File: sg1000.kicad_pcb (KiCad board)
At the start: 2 copper layers, 64 parts, among them CN1 Conn_01x07_Female, J1 USB-B1HSB6, J2 RCJ-014, J3 RCJ-013, Q1 2n4401, Q1c1 2n3906, SW1 Pause Key, SW2 Power Toggle, U1 SG-1000-Cart, U10 PLCCZ80, U100 74HCT574, U101 74HCT574, U102 74HCT574, U103 AS6C62256-DIP, U11 AS6C62256-DIP, U12 TMS9918A, U13 74LS139, U16 74LS32, U18 74LS257, U21 74LS257, U3 SN76489AN, U99 74HCT04, X2 10.73863MHz

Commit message: This routing is gonna kill me
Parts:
- moved U16 103.4 mm to (65.6, 137.0), turned to -90 degrees
- moved U13 22.0 mm to (68.2, 149.2), turned to -90 degrees
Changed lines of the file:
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@@
   )
   (footprint "Package_DIP:DIP-16_W7.62mm_LongPads" (layer "F.Cu")
-    (at 76.962 129.032 180)
+    (at 68.16 149.175 -90)
     (descr "16-lead though-hole mounted DIP package, row spacing 7.62 mm (300 mils), LongPads")
     (tags "THT DIP DIL PDIP 2.54mm 7.62mm 300mil LongPads")
@@
     (property "Sheetname" "")
     (attr through_hole)
-    (fp_text reference "U13" (at 3.81 -2.33) (layer "F.SilkS")
+    (fp_text reference "U13" (at 3.81 -2.33 -270) (layer "F.SilkS")
       (effects (font (size 1 1) (thickness 0.15)))
     )
-    (fp_text value "74LS139" (at 3.81 20.11) (layer "F.Fab")
+    (fp_text value "74LS139" (at 3.81 20.11 -270) (layer "F.Fab")
       (effects (font (size 1 1) (thickness 0.15)))
     )
-    (fp_text user "${REFERENCE}" (at 3.81 8.89) (layer "F.Fab")
+    (fp_text user "${REFERENCE}" (at 3.81 8.89 -270) (layer "F.Fab")
       (effects (font (size 1 1) (thickness 0.15)))
     )
@@
     (fp_line (start 6.985 19.05) (end 0.635 19.05) (layer "F.Fab") (width 0.1))
     (fp_line (start 6.985 -1.27) (end 6.985 19.05) (layer "F.Fab") (width 0.1))
-    (pad "1" thru_hole rect (at 0 0 180) (size 2.4 1.6) (drill 0.8) (layers *.Cu *.Mask)
+    (pad "1" thru_hole rect (at 0 0 270) (size 2.4 1.6) (drill 0.8) (layers *.Cu *.Mask)
       (net 43 "/~{MREQ}") (pinfunction "E") (pintype "input"))
-    (pad "2" thru_hole oval (at 0 2.54 180) (size 2.4 1.6) (drill 0.8) (layers *.Cu *.Mask)
+    (pad "2" thru_hole oval (at 0 2.54 270) (size 2.4 1.6) (drill 0.8) (layers *.Cu *.Mask)
       (net 22 "/A14") (pinfunction "A0") (pintype "input"))
-    (pad "3" thru_hole oval (at 0 5.08 180) (size 2.4 1.6) (drill 0.8) (layers *.Cu *.Mask)
+    (pad "3" thru_hole oval (at 0 5.08 270) (size 2.4 1.6) (drill 0.8) (layers *.Cu *.Mask)
       (net 24 "/A15") (pinfunction "A1") (pintype "input"))
-    (pad "4" thru_hole oval (at 0 7.62 180) (size 2.4 1.6) (drill 0.8) (layers *.Cu *.Mask)
+    (pad "4" thru_hole oval (at 0 7.62 270) (size 2.4 1.6) (drill 0.8) (layers *.Cu *.Mask)
       (net 99 "unconnected-(U13-Pad4)") (pinfunction "O0") (pintype "output+no_connect"))
-    (pad "5" thru_hole oval (at 0 10.16 180) (size 2.4 1.6) (drill 0.8) (layers *.Cu *.Mask)
+    (pad "5" thru_hole oval (at 0 10.16 270) (size 2.4 1.6) (drill 0.8) (layers *.Cu *.Mask)
       (net 97 "unconnected-(U13-Pad5)") (pinfunction "O1") (pintype "output+no_connect"))
-    (pad "6" thru_hole oval (at 0 12.7 180) (size 2.4 1.6) (drill 0.8) (layers *.Cu *.Mask)
+    (pad "6" thru_hole oval (at 0 12.7 270) (size 2.4 1.6) (drill 0.8) (layers *.Cu *.Mask)
       (net 45 "/~{EXM1}") (pinfunction "O2") (pintype "output"))
-    (pad "7" thru_hole oval (at 0 15.24 180) (size 2.4 1.6) (drill 0.8) (layers *.Cu *.Mask)
+    (pad "7" thru_hole oval (at 0 15.24 270) (size 2.4 1.6) (drill 0.8) (layers *.Cu *.Mask)
       (net 44 "Net-(R9-Pad2)") (pinfunction "O3") (pintype "output"))
-    (pad "8" thru_hole oval (at 0 17.78 180) (size 2.4 1.6) (drill 0.8) (layers *.Cu *.Mask)
+    (pad "8" thru_hole oval (at 0 17.78 270) (size 2.4 1.6) (drill 0.8) (layers *.Cu *.Mask)
       (net 1 "GND") (pinfunction "GND") (pintype "power_in"))
-    (pad "9" thru_hole oval (at 7.62 17.78 180) (size 2.4 1.6) (drill 0.8) (layers *.Cu *.Mask)
+    (pad "9" thru_hole oval (at 7.62 17.78 270) (size 2.4 1.6) (drill 0.8) (layers *.Cu *.Mask)
       (net 51 "/~{KB_SEL}") (pinfunction "O3") (pintype "output"))
-    (pad "10" thru_hole oval (at 7.62 15.24 180) (size 2.4 1.6) (drill 0.8) (layers *.Cu *.Mask)
+    (pad "10" thru_hole oval (at 7.62 15.24 270) (size 2.4 1.6) (drill 0.8) (layers *.Cu *.Mask)
       (net 50 "Net-(U13-Pad10)") (pinfunction "O2") (pintype "output"))
-    (pad "11" thru_hole oval (at 7.62 12.7 180) (size 2.4 1.6) (drill 0.8) (layers *.Cu *.Mask)
+    (pad "11" thru_hole oval (at 7.62 12.7 270) (size 2.4 1.6) (drill 0.8) (layers *.Cu *.Mask)
       (net 49 "Net-(R4-Pad1)") (pinfunction "O1") (pintype "output"))
-    (pad "12" thru_hole oval (at 7.62 10.16 180) (size 2.4 1.6) (drill 0.8) (layers *.Cu *.Mask)
+    (pad "12" thru_hole oval (at 7.62 10.16 270) (size 2.4 1.6) (drill 0.8) (layers *.Cu *.Mask)
       (net 98 "unconnected-(U13-Pad12)") (pinfunction "O0") (pintype "output+no_connect"))
-    (pad "13" thru_hole oval (at 7.62 7.62 180) (size 2.4 1.6) (drill 0.8) (layers *.Cu *.Mask)
+    (pad "13" thru_hole oval (at 7.62 7.62 270) (size 2.4 1.6) (drill 0.8) (layers *.Cu *.Mask)
       (net 18 "/A7") (pinfunction "A1") (pintype "input"))
-    (pad "14" thru_hole oval (at 7.62 5.08 180) (size 2.4 1.6) (drill 0.8) (layers *.Cu *.Mask)
+    (pad "14" thru_hole oval (at 7.62 5.08 270) (size 2.4 1.6) (drill 0.8) (layers *.Cu *.Mask)
       (net 20 "/A6") (pinfunction "A0") (pintype "input"))
-    (pad "15" thru_hole oval (at 7.62 2.54 180) (size 2.4 1.6) (drill 0.8) (layers *.Cu *.Mask)
+    (pad "15" thru_hole oval (at 7.62 2.54 270) (size 2.4 1.6) (drill 0.8) (layers *.Cu *.Mask)
       (net 35 "/~{IORQ}") (pinfunction "E") (pintype "input"))
-    (pad "16" thru_hole oval (at 7.62 0 180) (size 2.4 1.6) (drill 0.8) (layers *.Cu *.Mask)
+    (pad "16" thru_hole oval (at 7.62 0 270) (size 2.4 1.6) (drill 0.8) (layers *.Cu *.Mask)
       (net 2 "+5V") (pinfunction "VCC") (pintype "power_in"))
     (model "${KICAD6_3DMODEL_DIR}/Package_DIP.3dshapes/DIP-16_W7.62mm.wrl"
@@
   )
   (footprint "Package_DIP:DIP-14_W7.62mm_LongPads" (layer "F.Cu")
-    (at 165.085 108.58)
+    (at 65.62 137 -90)
     (descr "14-lead though-hole mounted DIP package, row spacing 7.62 mm (300 mils), LongPads")
     (tags "THT DIP DIL PDIP 2.54mm 7.62mm 300mil LongPads")
@@
     (property "Sheetname" "")
     (attr through_hole)
-    (fp_text reference "U16" (at 3.81 -2.33) (layer "F.SilkS")
+    (fp_text reference "U16" (at 3.81 -2.33 90) (layer "F.SilkS")
       (effects (font (size 1 1) (thickness 0.15)))
     )
-    (fp_text value "74LS32" (at 3.81 17.57) (layer "F.Fab")
+    (fp_text value "74LS32" (at 3.81 17.57 90) (layer "F.Fab")
       (effects (font (size 1 1) (thickness 0.15)))
     )
-    (fp_text user "${REFERENCE}" (at 3.81 7.62) (layer "F.Fab")
+    (fp_text user "${REFERENCE}" (at 3.81 7.62 90) (layer "F.Fab")
       (effects (font (size 1 1) (thickness 0.15)))
     )
@@
     (fp_line (start 0.635 16.51) (end 0.635 -0.27) (layer "F.Fab") (width 0.1))
     (fp_line (start 6.985 16.51) (end 0.635 16.51) (layer "F.Fab") (width 0.1))
-    (pad "1" thru_hole rect (at 0 0) (size 2.4 1.6) (drill 0.8) (layers *.Cu *.Mask)
+    (pad "1" thru_hole rect (at 0 0 270) (size 2.4 1.6) (drill 0.8) (layers *.Cu *.Mask)
       (net 50 "Net-(U13-Pad10)") (pintype "input"))
-    (pad "2" thru_hole oval (at 0 2.54) (size 2.4 1.6) (drill 0.8) (layers *.Cu *.Mask)
+    (pad "2" thru_hole oval (at 0 2.54 270) (size 2.4 1.6) (drill 0.8) (layers *.Cu *.Mask)
       (net 29 "/~{RD}") (pintype "input"))
-    (pad "3" thru_hole oval (at 0 5.08) (size 2.4 1.6) (drill 0.8) (layers *.Cu *.Mask)
+    (pad "3" thru_hole oval (at 0 5.08 270) (size 2.4 1.6) (drill 0.8) (layers *.Cu *.Mask)
       (net 54 "/~{VDP_RD}") (pintype "output"))
-    (pad "4" thru_hole oval (at 0 7.62) (size 2.4 1.6) (drill 0.8) (layers *.Cu *.Mask)
+    (pad "4" thru_hole oval (at 0 7.62 270) (size 2.4 1.6) (drill 0.8) (layers *.Cu *.Mask)
       (net 50 "Net-(U13-Pad10)") (pintype "input"))
-    (pad "5" thru_hole oval (at 0 10.16) (size 2.4 1.6) (drill 0.8) (layers *.Cu *.Mask)
+    (pad "5" thru_hole oval (at 0 10.16 270) (size 2.4 1.6) (drill 0.8) (layers *.Cu *.Mask)
       (net 30 "/~{WR}") (pintype "input"))
-    (pad "6" thru_hole oval (at 0 12.7) (size 2.4 1.6) (drill 0.8) (layers *.Cu *.Mask)
+    (pad "6" thru_hole oval (at 0 12.7 270) (size 2.4 1.6) (drill 0.8) (layers *.Cu *.Mask)
       (net 52 "/~{VDP_WR}") (pintype "output"))
-    (pad "7" thru_hole oval (at 0 15.24) (size 2.4 1.6) (drill 0.8) (layers *.Cu *.Mask)
+    (pad "7" thru_hole oval (at 0 15.24 270) (size 2.4 1.6) (drill 0.8) (layers *.Cu *.Mask)
       (net 1 "GND") (pinfunction "GND") (pintype "power_in"))
-    (pad "8" thru_hole oval (at 7.62 15.24) (size 2.4 1.6) (drill 0.8) (layers *.Cu *.Mask)
+    (pad "8" thru_hole oval (at 7.62 15.24 270) (size 2.4 1.6) (drill 0.8) (layers *.Cu *.Mask)
       (net 55 "Net-(R15-Pad2)") (pintype "output"))
-    (pad "9" thru_hole oval (at 7.62 12.7) (size 2.4 1.6) (drill 0.8) (layers *.Cu *.Mask)
+    (pad "9" thru_hole oval (at 7.62 12.7 270) (size 2.4 1.6) (drill 0.8) (layers *.Cu *.Mask)
       (net 51 "/~{KB_SEL}") (pintype "input"))
-    (pad "10" thru_hole oval (at 7.62 10.16) (size 2.4 1.6) (drill 0.8) (layers *.Cu *.Mask)
+    (pad "10" thru_hole oval (at 7.62 10.16 270) (size 2.4 1.6) (drill 0.8) (layers *.Cu *.Mask)
       (net 29 "/~{RD}") (pintype "input"))
-    (pad "11" thru_hole oval (at 7.62 7.62) (size 2.4 1.6) (drill 0.8) (layers *.Cu *.Mask)
+    (pad "11" thru_hole oval (at 7.62 7.62 270) (size 2.4 1.6) (drill 0.8) (layers *.Cu *.Mask)
       (net 53 "/~{EXM2}") (pintype "output"))
-    (pad "12" thru_hole oval (at 7.62 5.08) (size 2.4 1.6) (drill 0.8) (layers *.Cu *.Mask)
+    (pad "12" thru_hole oval (at 7.62 5.08 270) (size 2.4 1.6) (drill 0.8) (layers *.Cu *.Mask)
       (net 24 "/A15") (pintype "input"))
-    (pad "13" thru_hole oval (at 7.62 2.54) (size 2.4 1.6) (drill 0.8) (layers *.Cu *.Mask)
+    (pad "13" thru_hole oval (at 7.62 2.54 270) (size 2.4 1.6) (drill 0.8) (layers *.Cu *.Mask)
       (net 43 "/~{MREQ}") (pintype "input"))
-    (pad "14" thru_hole oval (at 7.62 0) (size 2.4 1.6) (drill 0.8) (layers *.Cu *.Mask)
+    (pad "14" thru_hole oval (at 7.62 0 270) (size 2.4 1.6) (drill 0.8) (layers *.Cu *.Mask)
       (net 2 "+5V") (pinfunction "VCC") (pintype "power_in"))
     (model "${KICAD6_3DMODEL_DIR}/Package_DIP.3dshapes/DIP-14_W7.62mm.wrl"

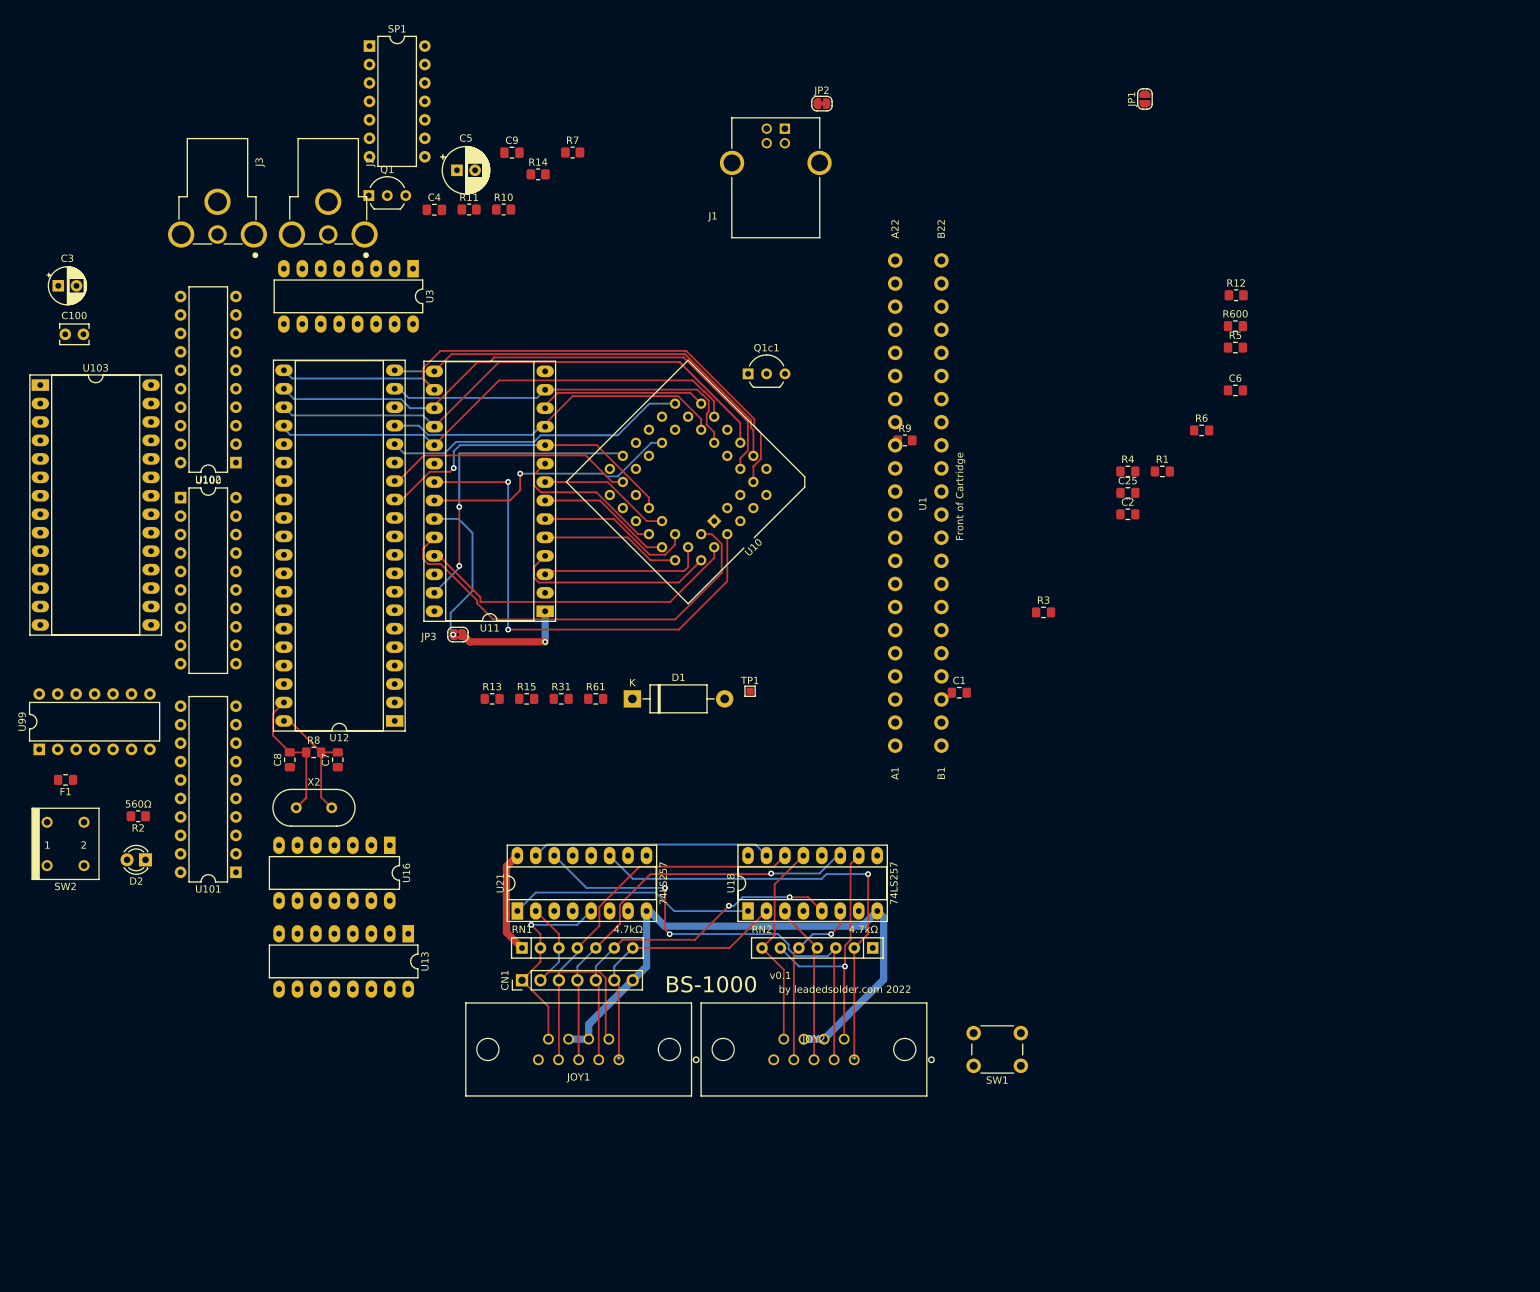
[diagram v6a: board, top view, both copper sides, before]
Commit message: Starting route all over again
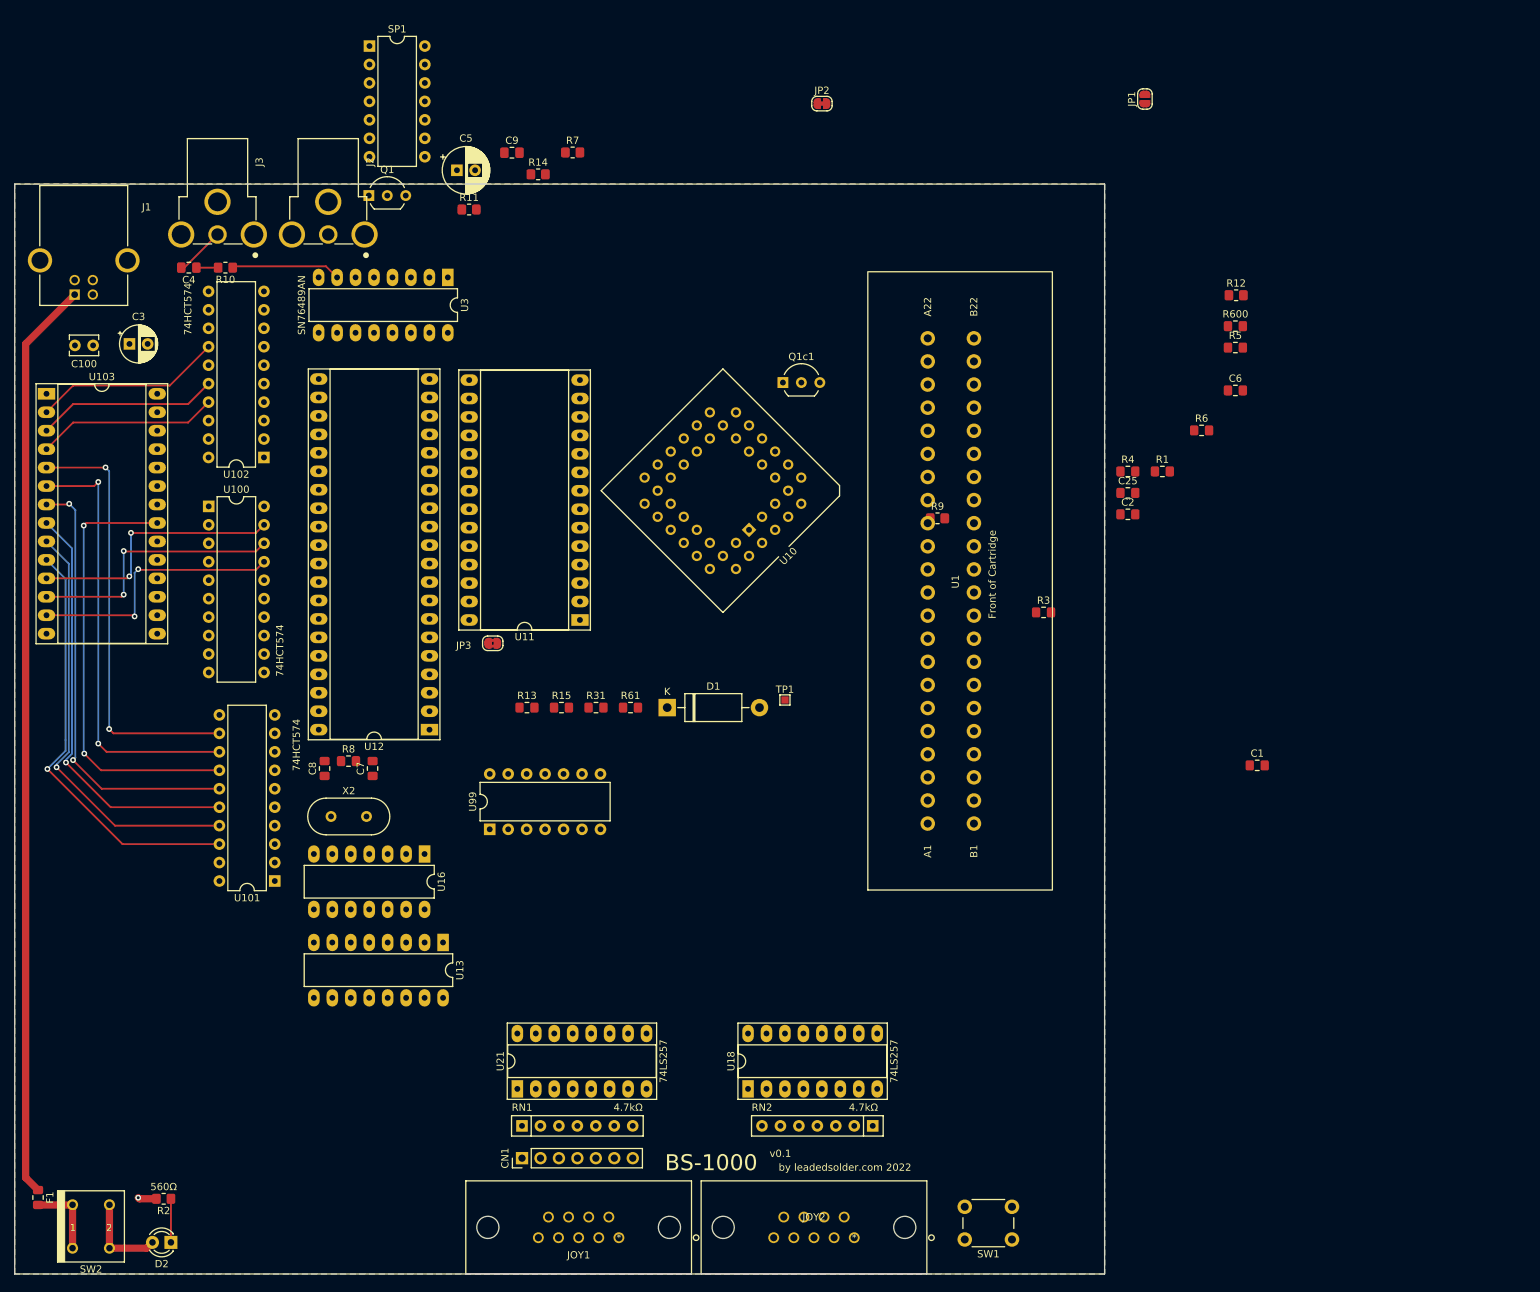
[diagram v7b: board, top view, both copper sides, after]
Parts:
- moved J1 96.2 mm to (23.5, 56.5), turned to 180 degrees
- moved U99 63.0 mm to (79.4, 134.8)
- moved F1 57.6 mm to (17.2, 185.5), turned to -90 degrees
- moved D2 52.8 mm to (35.5, 191.7)
- moved R2 52.8 mm to (34.5, 185.7)
- moved SW2 52.8 mm to (24.5, 189.7)
- moved C1 42.2 mm to (185.0, 126.0)
- moved R10 39.1 mm to (43.0, 57.5), turned to 180 degrees
- moved C4 34.7 mm to (38.0, 57.5), turned to 180 degrees
- moved CN1 24.5 mm to (83.8, 180.1)
- moved JOY1 24.5 mm to (97.2, 191.0)
- moved JOY2 24.5 mm to (129.5, 191.0)
- moved RN1 24.5 mm to (83.8, 175.6)
- moved RN2 24.5 mm to (132.1, 175.6)
- moved U18 24.5 mm to (114.9, 170.5)
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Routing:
- net /USB_Power: track 0.00 -> 126.7 mm
- net GND: track 97.5 -> 2.56 mm
- net /D4: track 85.3 -> 0.00 mm
- net /D5: track 78.7 -> 0.00 mm
- net /A0: track 77.7 -> 0.00 mm, vias 1 -> 0
- net /D6: track 73.8 -> 0.00 mm
- net /A10: track 69.9 -> 0.00 mm, vias 2 -> 0
- net /D7: track 67.5 -> 0.00 mm
- net /JOY2_DOWN: track 64.2 -> 0.00 mm, vias 2 -> 0
- net /JOY2_UP: track 63.5 -> 0.00 mm, vias 1 -> 0
- net /VRAM_A4: track 0.00 -> 61.2 mm, vias 0 -> 2
- net /VRAM_A3: track 0.00 -> 60.7 mm, vias 0 -> 2
- net /VRAM_A5: track 0.00 -> 60.5 mm, vias 0 -> 2
- net /VRAM_A6: track 0.00 -> 59.8 mm, vias 0 -> 2
- net /D3: track 58.9 -> 0.00 mm
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- added copper zone on F.Cu, net +5V
- added copper zone on B.Cu, net GND
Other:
- board outline added: 150 x 150 mm
- board text removed: "TODO: Figure out the keepout for an entire cartridge"

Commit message: Most of the route done
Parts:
- moved R600 130.7 mm to (51.4, 59.7), turned to -90 degrees
- moved C3 111.2 mm to (23.5, 179.0)
- moved JP2 99.3 mm to (150.7, 130.8), turned to 180 degrees
- moved C25 97.1 mm to (76.2, 54.6)
- moved R1 82.3 mm to (96.3, 117.9), turned to 180 degrees
- moved R61 71.9 mm to (51.4, 63.9), turned to 90 degrees
- moved R31 70.8 mm to (76.2, 49.5), turned to 180 degrees
- moved R5 65.2 mm to (116.8, 69.1)
- moved R6 56.9 mm to (121.5, 68.8)
- moved R3 56.5 mm to (100.6, 117.9)
- moved R12 55.5 mm to (128.0, 73.9), turned to -90 degrees
- moved U99 52.8 mm to (35.3, 163.8), turned to 180 degrees
- moved TP1 46.7 mm to (106.9, 72.1)
- moved JP1 43.6 mm to (159.5, 76.7), turned to 180 degrees
- moved U16 27.4 mm to (44.9, 148.3), turned to 0 degrees
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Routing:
- net /~{WR}: track 0.00 -> 185.5 mm, vias 0 -> 5
- net +5V: track 12.2 -> 170.5 mm, vias 0 -> 7
- net /CLK: track 0.00 -> 137.6 mm, vias 0 -> 2
- net /A0: track 0.00 -> 131.2 mm, vias 0 -> 3
- net /~{RD}: track 0.00 -> 129.6 mm, vias 0 -> 5
- net /CON: track 0.00 -> 128.7 mm, vias 0 -> 3
- net /AD7: track 0.00 -> 118.8 mm, vias 0 -> 6
- net /D4: track 0.00 -> 117.9 mm, vias 0 -> 3
- net /D5: track 0.00 -> 116.1 mm, vias 0 -> 2
- net /D6: track 0.00 -> 112.2 mm, vias 0 -> 2
- net /D7: track 0.00 -> 110.6 mm, vias 0 -> 2
- net /D3: track 0.00 -> 104.2 mm, vias 0 -> 3
- net /D0: track 0.00 -> 103.7 mm, vias 0 -> 2
- net /D1: track 0.00 -> 98.6 mm, vias 0 -> 3
- net /A10: track 0.00 -> 98.2 mm, vias 0 -> 3
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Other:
- board text added: "Enable A15 to cart"
- board text added: "WRAM_A11"
